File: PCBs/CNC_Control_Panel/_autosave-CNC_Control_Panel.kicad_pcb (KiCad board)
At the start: 2 copper layers, 100 x 100 mm, 44 parts, among them J1 Conn_01x07_Male, J2 Conn_01x03_Male, P1 Conn_02x20_Odd_Even, X0 SW_Push, Y0 SW_Push

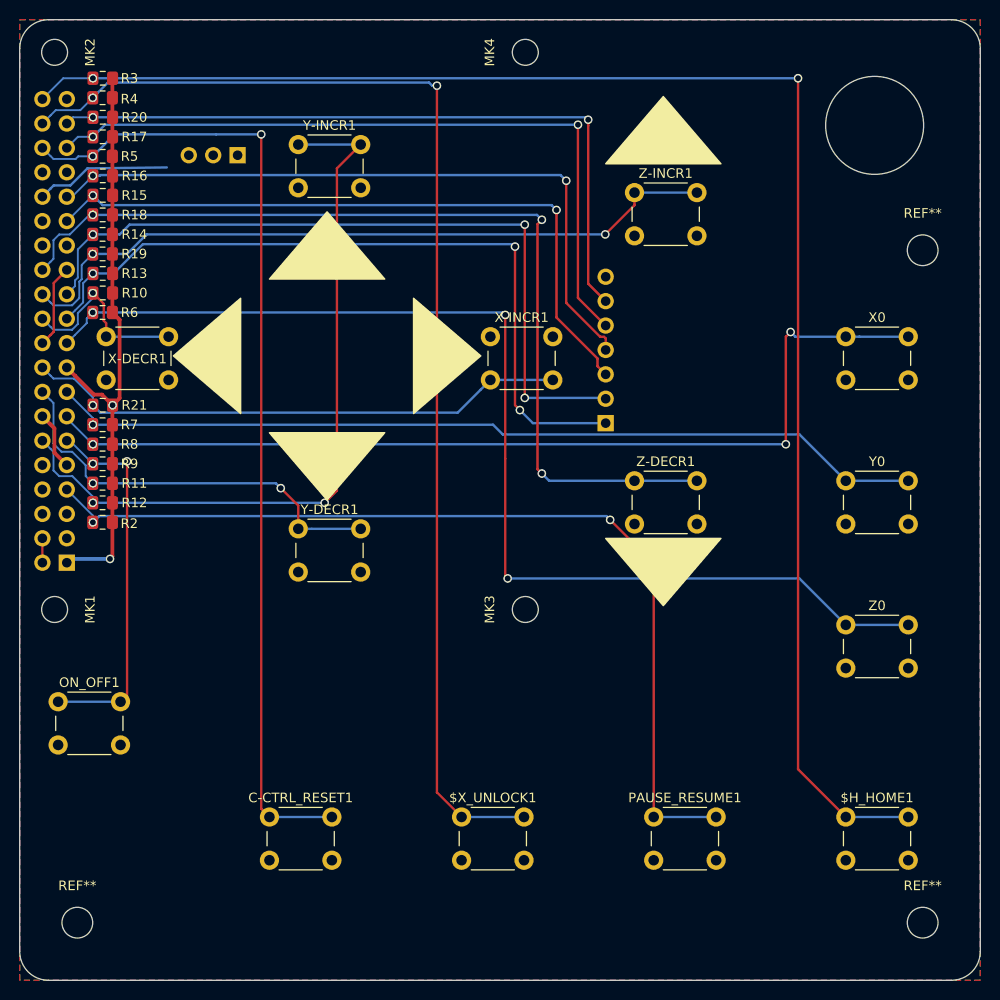
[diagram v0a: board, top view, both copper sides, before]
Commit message: added better silkscreen labeling & logo
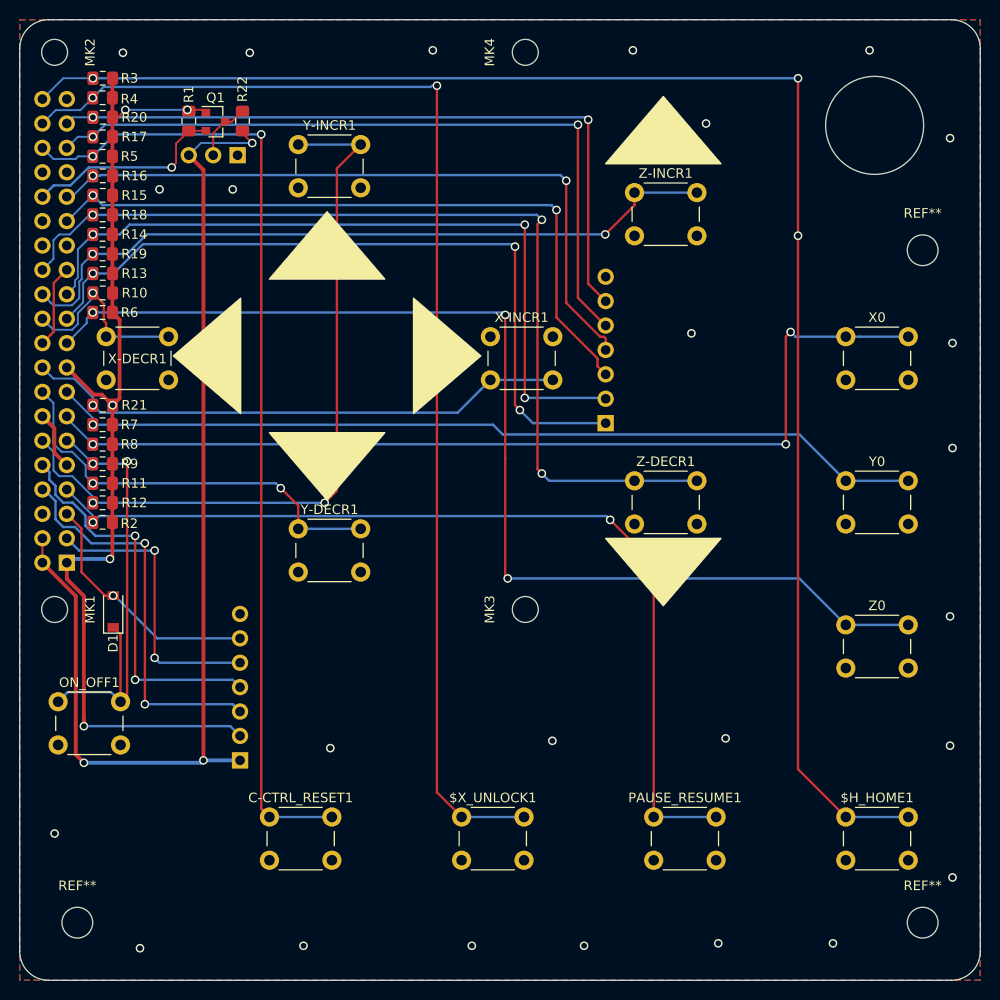
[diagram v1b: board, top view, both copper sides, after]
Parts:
- added D1: 1N4148W, Diode_SMD:D_SOD-123, F.Cu at (44.0, 139.1)
- added J3: Conn_01x07_Male, Connector_PinHeader_2.54mm:PinHeader_1x07_P2.54mm_Horizontal, B.Cu at (57.2, 154.6)
- added Q1: BSS138, Package_TO_SOT_SMD:SOT-23, F.Cu at (54.7, 88.1)
- added R1: 10k, Resistor_SMD:R_0805_2012Metric_Pad1.15x1.40mm_HandSolder, F.Cu at (51.9, 88.0)
- added R22: 10k, Resistor_SMD:R_0805_2012Metric_Pad1.15x1.40mm_HandSolder, F.Cu at (57.5, 88.0)
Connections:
- J2 pad 2: /GPIO12(PWM0) -> Net-(J2-Pad2)
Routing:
- net +5V: track 2.54 -> 114.0 mm, vias 0 -> 3
- net +3V3: track 61.8 -> 106.4 mm, vias 2 -> 5
- net /GPIO14(TXD0): track 0.00 -> 41.1 mm, vias 0 -> 2
- net /GPIO15(RXD0): track 0.00 -> 40.6 mm, vias 0 -> 2
- net /GPIO2(SDA1): track 0.00 -> 30.0 mm, vias 0 -> 2
- net /GPIO3(SCL1): track 0.00 -> 26.1 mm, vias 0 -> 1
- net /GPIO17(GEN0): track 39.2 -> 48.1 mm
- net /GPIO12(PWM0): track 14.2 -> 21.0 mm, vias 0 -> 1
- net Net-(J2-Pad2): track 0.00 -> 6.30 mm
- net GND: vias 0 -> 25
- net /GPIO21(SPI1_SCK): vias 2 -> 3
